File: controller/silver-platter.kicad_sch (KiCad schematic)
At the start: 61 parts, among them J1 UART, J11 LED1_B, J12 LED1_G, J13 LED1_R, J14 LED_ANODE, J15 LED2_B, J16 LED2_G, J17 LED2_R, J19 RX_VDD, J2 JTAG/SWJ, J20 RX_iBUS, J21 RX_GND, J22 BOOT, J23 +BATT, J24 -BATT, J3 VDD_ACC, J4 SCL_ACC, J5 SDA_ACC, J6 GND_ACC, J8 CH1_ESC, J9 CH2_ESC, Q1 Q_NMOS, Q2 Q_NMOS, Q3 Q_NMOS, SW1 SW_Push, U1 STM32F205RETx, U2 TLV74033PDBVR, U3 LMR50410Y5FQDBVRQ1

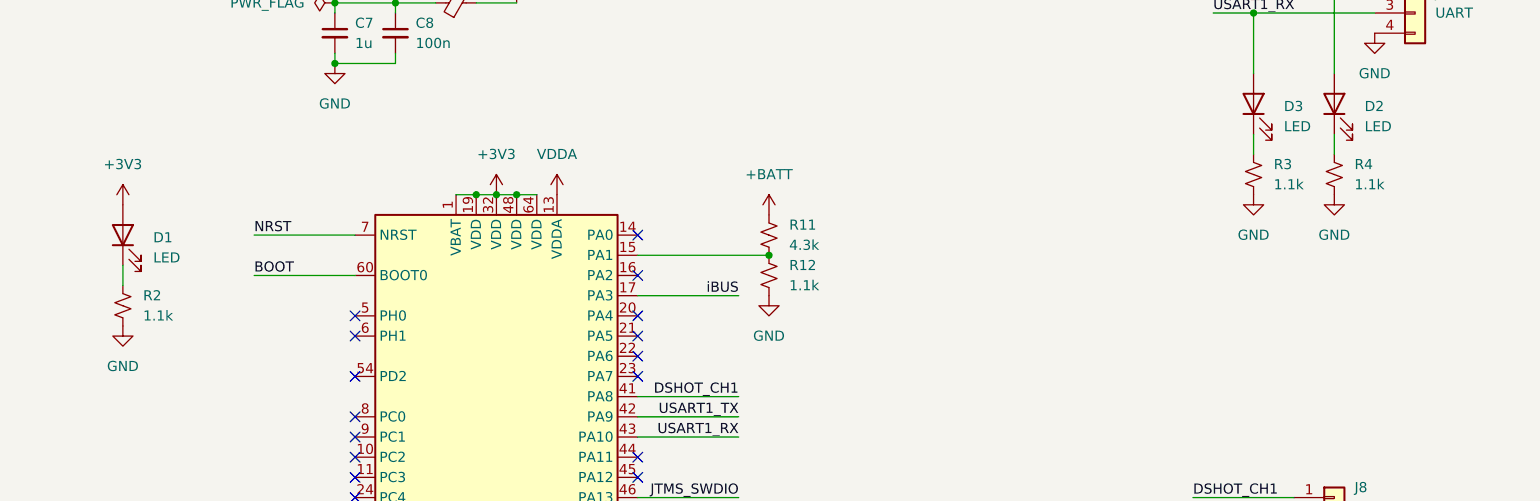
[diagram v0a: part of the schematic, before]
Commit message: Indicator LED resistors from 1.1k to 4.3k
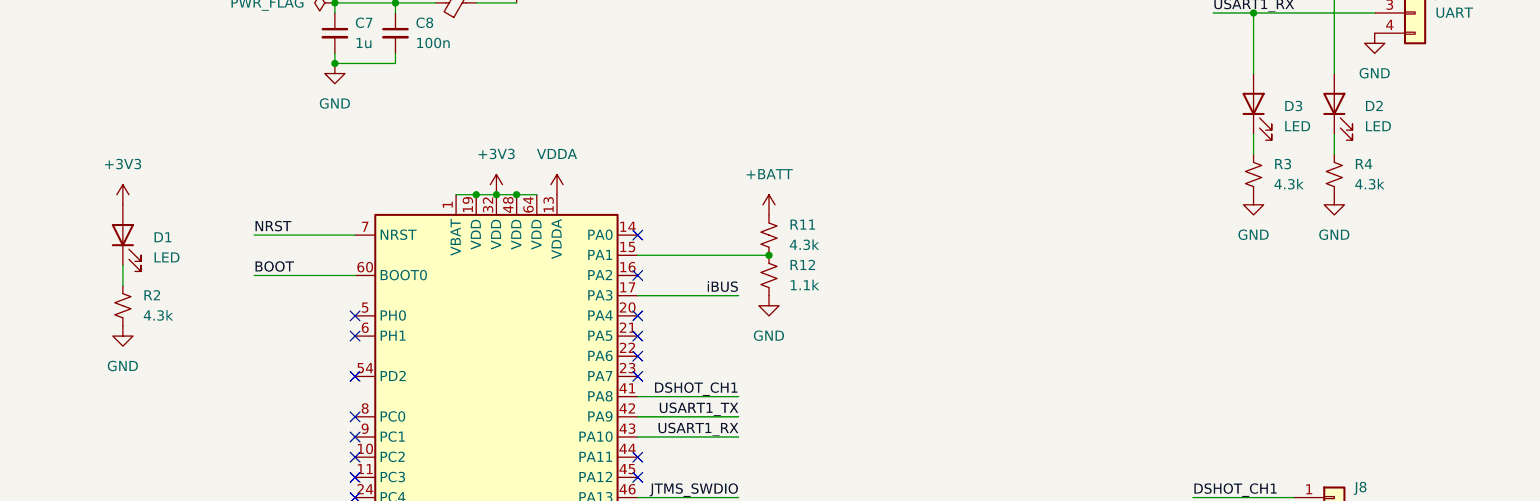
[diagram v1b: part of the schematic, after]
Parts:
- R2, R3, R4: value 1.1k -> 4.3k
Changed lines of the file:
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@@
 			)
 		)
-		(property "Value" "1.1k"
+		(property "Value" "4.3k"
 			(at 284.48 99.0599 0)
 			(effects
@@
 			)
 		)
-		(property "Value" "1.1k"
+		(property "Value" "4.3k"
 			(at 142.24 115.5699 0)
 			(effects
@@
 			)
 		)
-		(property "Value" "1.1k"
+		(property "Value" "4.3k"
 			(at 294.64 99.0599 0)
 			(effects
